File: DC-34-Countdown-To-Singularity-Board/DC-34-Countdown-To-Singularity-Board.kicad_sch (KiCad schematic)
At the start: 22 parts, among them SW1 SW_DIP_x01, U1 LM7805_TO220, Y1 Crystal

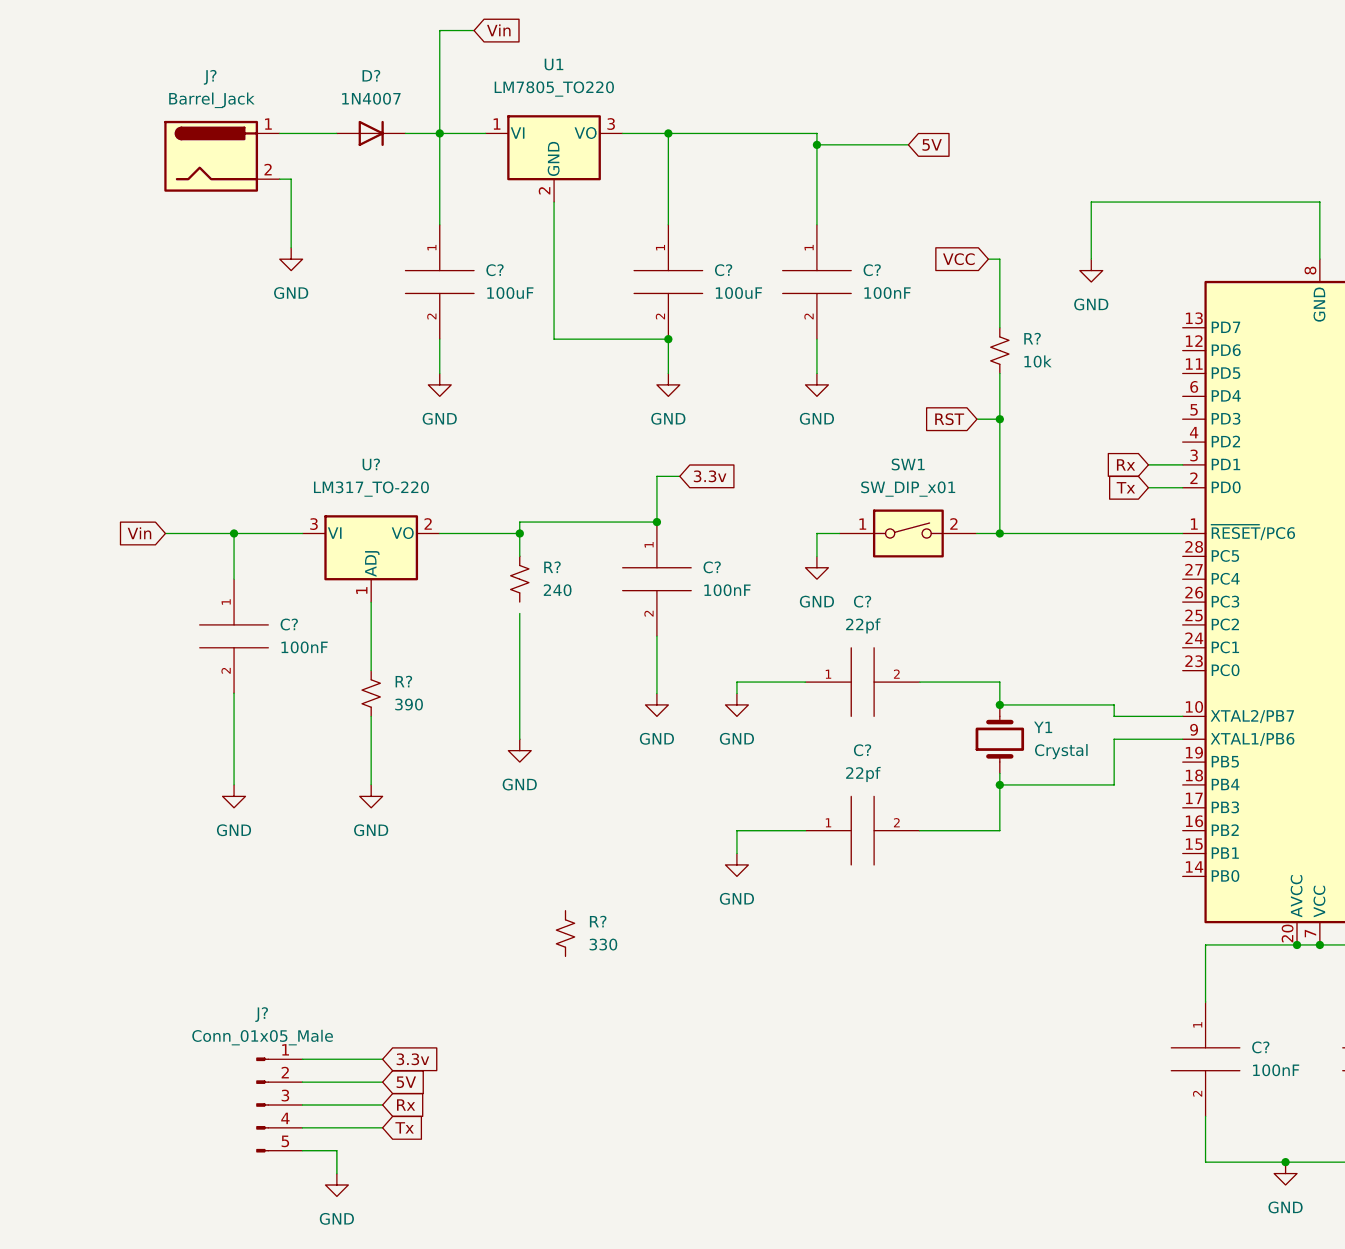
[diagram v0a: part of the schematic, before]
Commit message: Added LEDs
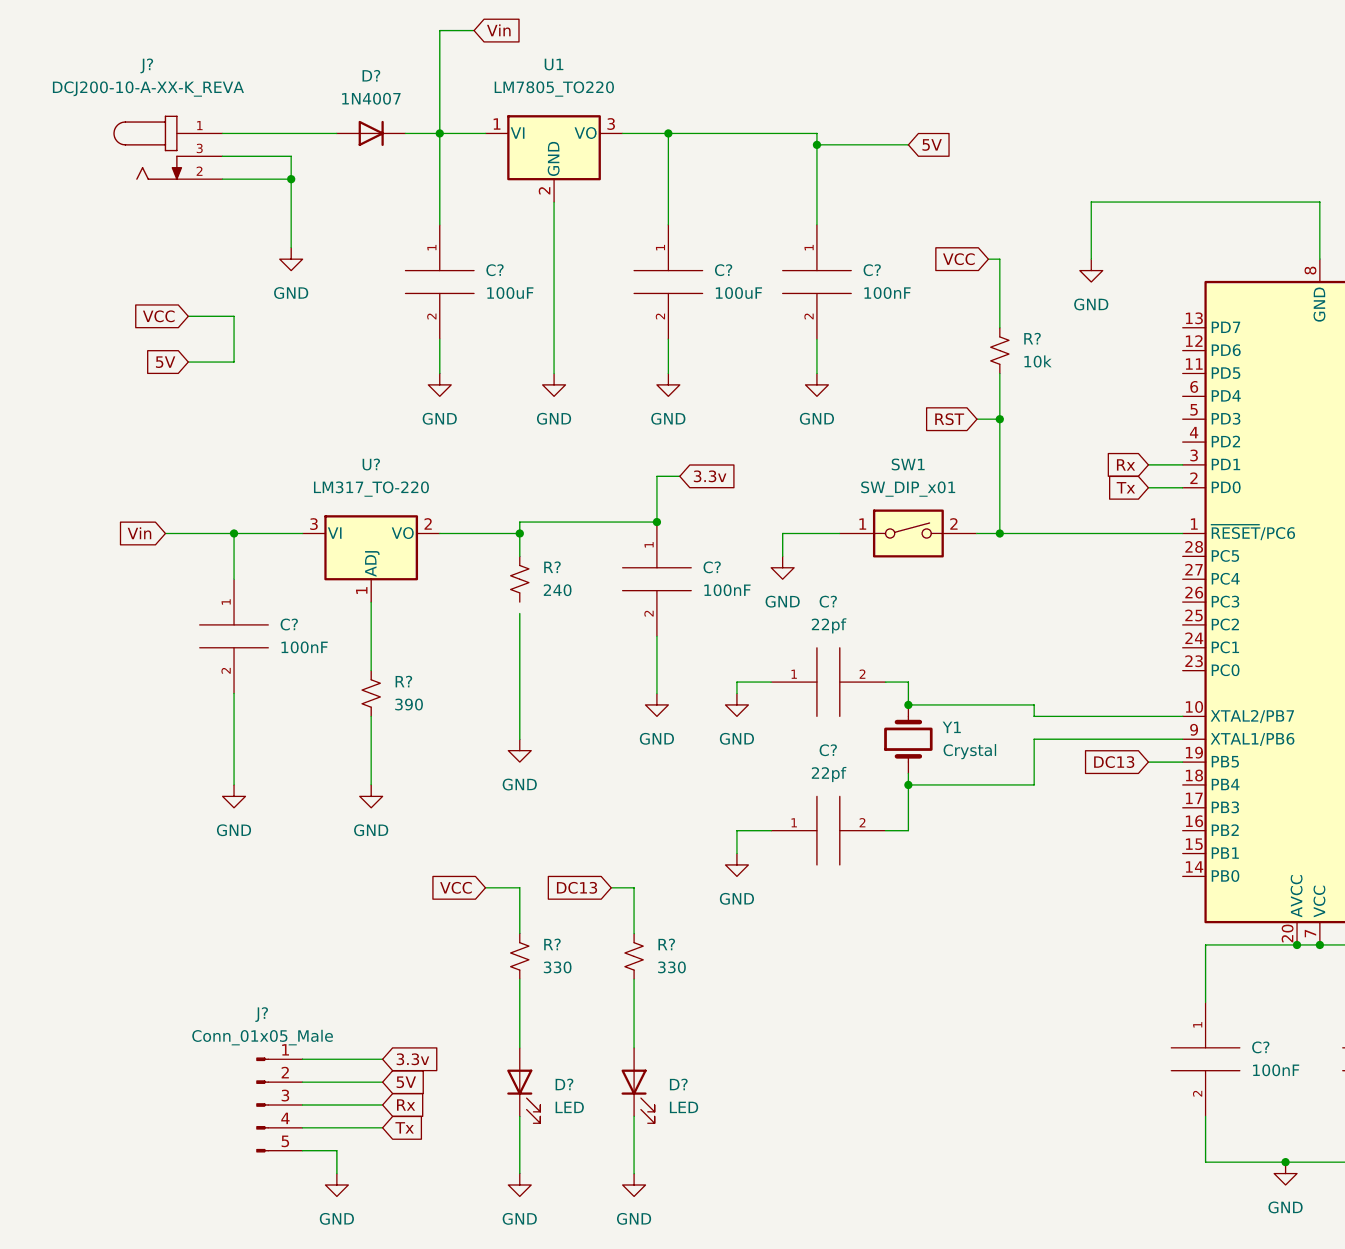
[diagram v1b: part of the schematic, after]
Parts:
- removed J?: Barrel_Jack, symbol Connector:Barrel_Jack
- added D? (x2): LED, LED_THT:LED_D3.0mm, symbol Device:LED
- added J?: DCJ200-10-A-XX-K_REVA, DCJ200:GCT_DCJ200-10-A-XX-K_REVA, symbol DCJ200-10-A-XX-K_REVA:DCJ200-10-A-XX-K_REVA
- added R?: 330, Resistor_THT:R_Axial_DIN0207_L6.3mm_D2.5mm_P2.54mm_Vertical, symbol Device:R_Small_US
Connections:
- net VCC is gone; now on net 5V: J?.2 (Pin_2), R?.1
- net 5V: now also R?.1
- net GND: now also D?.1 (K), D?.1 (K), J?.2, J?.3
- net at D?.2 (A): now also J?.1
- net DC13: now reaches U?.19 (PB5)
- net DC13: now also R?.1
- net at R?.2: now also D?.2 (A)
- new net: D?.2 (A), R?.2
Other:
- moved on the sheet: C?, R?, Y1

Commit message: Finished first version of graphic.
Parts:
- added BT1: Battery_Cell, Battery:BatteryHolder_LINX_BAT-HLD-012-SMT, symbol Device:Battery_Cell
- added C3, C4: 10uF, Capacitor_THT:C_Radial_D10.0mm_H12.5mm_P5.00mm, symbol pspice:CAP
- added C8, C9: 100nF, Capacitor_THT:C_Radial_D10.0mm_H12.5mm_P5.00mm, symbol pspice:CAP
- added J10, J4, J5, J6, J7, J8, J9: Conn_01x06_Male, Connector_PinHeader_2.54mm:PinHeader_2x03_P2.54mm_Vertical, symbol Connector:Conn_01x06_Male
- added R11: 1k, Resistor_THT:R_Axial_DIN0207_L6.3mm_D2.5mm_P2.54mm_Vertical, symbol Device:R_Small_US
- added R12, R13, R15, R16: 10k, Resistor_THT:R_Axial_DIN0207_L6.3mm_D2.5mm_P2.54mm_Vertical, symbol Device:R_Small_US
- added R4, R5, R6, R7, R8, R9: 330, Resistor_THT:R_Axial_DIN0207_L6.3mm_D2.5mm_P2.54mm_Vertical, symbol Device:R_Small_US
- added SW2, SW3: SW_DIP_x01, Button_Switch_THT:SW_PUSH_6mm_H7.3mm, symbol Switch:SW_DIP_x01
- added U4: PCF8523T, Package_SO:SOIC-8_3.9x4.9mm_P1.27mm, symbol Timer_RTC:PCF8523T
- added U5, U6: CC56-12CGKWA, Display_7Segment:CA56-12CGKWA, symbol Display_Character:CC56-12CGKWA
- added X1: SG-3030CM, Oscillator:Oscillator_SMD_SeikoEpson_SG3030CM, symbol Oscillator:SG-3030CM
- gave numbers to parts that had none: 22
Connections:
- net SCK is gone; now on net DC13: J3.3 (Pin_3)
- net 5V: now also C4.1, J10.5 (Pin_5), J4.5 (Pin_5), J5.5 (Pin_5), J6.5 (Pin_5), J7.5 (Pin_5), J8.5 (Pin_5), J9.5 (Pin_5), R11.1, R12.1, R13.1, R15.1, R16.1, X1.4 (Vcc)
- net GND: now also R1.2, BT1.2 (-), C3.2, C4.2, C8.2, C9.2, J10.6 (Pin_6), J4.6 (Pin_6), J5.6 (Pin_6), J6.6 (Pin_6), J7.6 (Pin_6), J8.6 (Pin_6), J9.6 (Pin_6), U4.4 (VSS), X1.2 (GND)
- net MISO: now also U3.18 (PB4), U5.5 (g), U6.5 (g)
- net MOSI: now also U3.17 (PB3), U5.10 (f), U6.10 (f)
- net CC4: now reaches U3.11 (PD5)
- net CC4: now also R9.1
- net a: now reaches U3.12 (PD6)
- net a: now also U5.11 (a), U6.11 (a)
- net b: now reaches U3.13 (PD7)
- net b: now also U5.7 (b), U6.7 (b)
- net c: now reaches U3.14 (PB0)
- net c: now also U5.4 (c), U6.4 (c)
- net d: now reaches U3.15 (PB1)
- net d: now also U5.2 (d), U6.2 (d)
- net e: now reaches U3.16 (PB2)
- net e: now also U5.1 (e), U6.1 (e)
- net CC5: now reaches U3.23 (PC0)
- net CC5: now also R4.1
- net CC6: now reaches U3.24 (PC1)
- net CC6: now also R5.1
- net UP: now reaches U3.25 (PC2)
- net UP: now also C8.1, SW3.2
- net DOWN: now reaches U3.26 (PC3)
- net DOWN: now also C9.1, SW2.2
- net SDA: now reaches U3.27 (PC4)
- net SDA: now also R15.2, U4.5 (SDA)
- net SCL: now reaches U3.28 (PC5)
- net SCL: now also R16.2, U4.6 (SCL)
- net CC1: now reaches U3.4 (PD2)
- net CC1: now also R6.1
- net CC2: now reaches U3.5 (PD3)
- net CC2: now also R7.1
- net CC3: now reaches U3.6 (PD4)
- net CC3: now also R8.1
- new net: R13.2, SW2.1
- new net: U4.2 (OSCO), X1.1 (VIO)
- new net: U4.1 (OSCI), X1.3 (OUT)
- new net: R6.2, U6.12 (CC1)
- new net: R12.2, SW3.1
- new net: R9.2, U6.6 (CC4)
- new net: R8.2, U6.8 (CC3)
- new net: R7.2, U6.9 (CC2)
- new net: R5.2, U5.9 (CC2)
- new net: R4.2, U5.12 (CC1)
- new net: BT1.1 (+), U4.3 (VBAT)
- new net: C3.1, R11.2, U4.8 (VDD)

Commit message: Put SAOs to 3.3v.
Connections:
- net 3.3v: now also J10.5 (Pin_5), J4.5 (Pin_5), J5.5 (Pin_5), J6.5 (Pin_5), J7.5 (Pin_5), J8.5 (Pin_5), J9.5 (Pin_5)
- net 5V: no longer J10.5 (Pin_5), J4.5 (Pin_5), J5.5 (Pin_5), J6.5 (Pin_5), J7.5 (Pin_5), J8.5 (Pin_5), J9.5 (Pin_5)
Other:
- moved on the sheet: J7
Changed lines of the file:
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@@
     (stroke (width 0) (type default) (color 0 0 0 0))
   )
-  (wire (pts (xy 158.75 176.53) (xy 160.02 176.53))
-    (stroke (width 0) (type default) (color 0 0 0 0))
-  )
-  (wire (pts (xy 149.86 173.99) (xy 160.02 173.99))
+  (wire (pts (xy 146.05 172.72) (xy 147.32 172.72))
+    (stroke (width 0) (type default) (color 0 0 0 0))
+  )
+  (wire (pts (xy 137.16 170.18) (xy 147.32 170.18))
     (stroke (width 0) (type default) (color 0 0 0 0))
   )
@@
     )
   )
-  (global_label "VCC" (shape input) (at 269.24 127 180) (fields_autoplaced)
-    (effects (font (size 1.27 1.27)) (justify right))
-    (property "Intersheet References" "${INTERSHEET_REFS}" (id 0) (at 263.1983 126.9206 0)
+  (global_label "3.3v" (shape input) (at 269.24 127 180) (fields_autoplaced)
+    (effects (font (size 1.27 1.27)) (justify right))
+    (property "Intersheet References" "${INTERSHEET_REFS}" (id 0) (at 262.8355 126.9206 0)
       (effects (font (size 1.27 1.27)) (justify right) hide)
     )
@@
     )
   )
-  (global_label "VCC" (shape input) (at 43.18 175.26 180) (fields_autoplaced)
-    (effects (font (size 1.27 1.27)) (justify right))
-    (property "Intersheet References" "${INTERSHEET_REFS}" (id 0) (at 37.1383 175.1806 0)
+  (global_label "3.3v" (shape input) (at 43.18 175.26 180) (fields_autoplaced)
+    (effects (font (size 1.27 1.27)) (justify right))
+    (property "Intersheet References" "${INTERSHEET_REFS}" (id 0) (at 36.7755 175.1806 0)
       (effects (font (size 1.27 1.27)) (justify right) hide)
     )
@@
     )
   )
-  (global_label "VCC" (shape input) (at 236.22 144.78 180) (fields_autoplaced)
-    (effects (font (size 1.27 1.27)) (justify right))
-    (property "Intersheet References" "${INTERSHEET_REFS}" (id 0) (at 230.1783 144.7006 0)
+  (global_label "3.3v" (shape input) (at 236.22 144.78 180) (fields_autoplaced)
+    (effects (font (size 1.27 1.27)) (justify right))
+    (property "Intersheet References" "${INTERSHEET_REFS}" (id 0) (at 229.8155 144.7006 0)
       (effects (font (size 1.27 1.27)) (justify right) hide)
     )
@@
     )
   )
-  (global_label "VCC" (shape input) (at 259.08 144.78 180) (fields_autoplaced)
-    (effects (font (size 1.27 1.27)) (justify right))
-    (property "Intersheet References" "${INTERSHEET_REFS}" (id 0) (at 253.0383 144.7006 0)
+  (global_label "3.3v" (shape input) (at 259.08 144.78 180) (fields_autoplaced)
+    (effects (font (size 1.27 1.27)) (justify right))
+    (property "Intersheet References" "${INTERSHEET_REFS}" (id 0) (at 252.6755 144.7006 0)
       (effects (font (size 1.27 1.27)) (justify right) hide)
     )
@@
     )
   )
-  (global_label "VCC" (shape input) (at 62.23 175.26 180) (fields_autoplaced)
-    (effects (font (size 1.27 1.27)) (justify right))
-    (property "Intersheet References" "${INTERSHEET_REFS}" (id 0) (at 56.1883 175.1806 0)
+  (global_label "3.3v" (shape input) (at 62.23 175.26 180) (fields_autoplaced)
+    (effects (font (size 1.27 1.27)) (justify right))
+    (property "Intersheet References" "${INTERSHEET_REFS}" (id 0) (at 55.8255 175.1806 0)
       (effects (font (size 1.27 1.27)) (justify right) hide)
     )
@@
     )
   )
-  (global_label "VCC" (shape input) (at 22.86 175.26 180) (fields_autoplaced)
-    (effects (font (size 1.27 1.27)) (justify right))
-    (property "Intersheet References" "${INTERSHEET_REFS}" (id 0) (at 16.8183 175.1806 0)
+  (global_label "3.3v" (shape input) (at 22.86 175.26 180) (fields_autoplaced)
+    (effects (font (size 1.27 1.27)) (justify right))
+    (property "Intersheet References" "${INTERSHEET_REFS}" (id 0) (at 16.4555 175.1806 0)
       (effects (font (size 1.27 1.27)) (justify right) hide)
     )
@@
     )
   )
-  (global_label "VCC" (shape input) (at 158.75 176.53 180) (fields_autoplaced)
-    (effects (font (size 1.27 1.27)) (justify right))
-    (property "Intersheet References" "${INTERSHEET_REFS}" (id 0) (at 152.7083 176.4506 0)
+  (global_label "3.3v" (shape input) (at 146.05 172.72 180) (fields_autoplaced)
+    (effects (font (size 1.27 1.27)) (justify right))
+    (property "Intersheet References" "${INTERSHEET_REFS}" (id 0) (at 139.6455 172.6406 0)
       (effects (font (size 1.27 1.27)) (justify right) hide)
     )
@@
     (pin "2")
   )
-  (symbol (lib_id "Connector:Conn_01x06_Male") (at 165.1 181.61 180) (unit 1)
-    (in_bom yes) (on_board yes) (fields_autoplaced)
-    (property "Reference" "J7" (id 0) (at 166.37 179.0699 0)
+  (symbol (lib_id "Connector:Conn_01x06_Male") (at 152.4 177.8 180) (unit 1)
+    (in_bom yes) (on_board yes) (fields_autoplaced)
+    (property "Reference" "J7" (id 0) (at 153.67 175.2599 0)
       (effects (font (size 1.27 1.27)) (justify right))
     )
-    (property "Value" "Conn_01x06_Male" (id 1) (at 166.37 181.6099 0)
+    (property "Value" "Conn_01x06_Male" (id 1) (at 153.67 177.7999 0)
       (effects (font (size 1.27 1.27)) (justify right))
     )
-    (property "Footprint" "Connector_PinHeader_2.54mm:PinHeader_2x03_P2.54mm_Vertical" (id 2) (at 165.1 181.61 0)
-      (effects (font (size 1.27 1.27)) hide)
-    )
-    (property "Datasheet" "~" (id 3) (at 165.1 181.61 0)
+    (property "Footprint" "Connector_PinHeader_2.54mm:PinHeader_2x03_P2.54mm_Vertical" (id 2) (at 152.4 177.8 0)
+      (effects (font (size 1.27 1.27)) hide)
+    )
+    (property "Datasheet" "~" (id 3) (at 152.4 177.8 0)
       (effects (font (size 1.27 1.27)) hide)
     )
@@
     (pin "2")
   )
-  (symbol (lib_id "power:GND") (at 149.86 173.99 0) (unit 1)
-    (in_bom yes) (on_board yes) (fields_autoplaced)
-    (property "Reference" "#PWR?" (id 0) (at 149.86 180.34 0)
-      (effects (font (size 1.27 1.27)) hide)
-    )
-    (property "Value" "GND" (id 1) (at 149.86 179.07 0))
-    (property "Footprint" "" (id 2) (at 149.86 173.99 0)
-      (effects (font (size 1.27 1.27)) hide)
-    )
-    (property "Datasheet" "" (id 3) (at 149.86 173.99 0)
-      (effects (font (size 1.27 1.27)) hide)
-    )
+  (symbol (lib_id "power:GND") (at 137.16 170.18 0) (unit 1)
+    (in_bom yes) (on_board yes) (fields_autoplaced)
+    (property "Reference" "#PWR?" (id 0) (at 137.16 176.53 0)
+      (effects (font (size 1.27 1.27)) hide)
+    )
+    (property "Value" "GND" (id 1) (at 137.16 175.26 0))
+    (property "Footprint" "" (id 2) (at 137.16 170.18 0)
+      (effects (font (size 1.27 1.27)) hide)
+    )
+    (property "Datasheet" "" (id 3) (at 137.16 170.18 0)
+      (effects (font (size 1.27 1.27)) hide)
+    )
